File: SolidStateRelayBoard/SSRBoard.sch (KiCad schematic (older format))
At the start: 54 parts, among them J101 CONN_01X02, J102 CONN_01X02, J103 CONN_01X02, J104 CONN_01X02, J105 CONN_01X02, J106 CONN_01X02, J107 CONN_01X02, J108 CONN_01X02, J109 CONN_01X02, J110 CONN_01X02, J111 CONN_01X02, J112 CONN_01X02, J113 CONN_01X02, J114 CONN_01X02, J115 CONN_01X02, J116 CONN_01X02, J117 CONN_01X02, J118 CONN_01X02, J119 CONN_01X02, J120 CONN_01X02, J121 CONN_01X02, J122 CONN_01X02, J123 CONN_01X02, J124 CONN_01X02, J125 CONN_01X02, J126 CONN_01X02, J127 CONN_01X02, J128 CONN_01X02, J129 CONN_01X02, J130 CONN_01X02, J131 CONN_01X02, J132 CONN_01X02, J134 CONN_01X02, J135 MOUNTING_HOLE, J136 MOUNTING_HOLE, J137 MOUNTING_HOLE, J138 MOUNTING_HOLE, U101 LEDDriverSSR

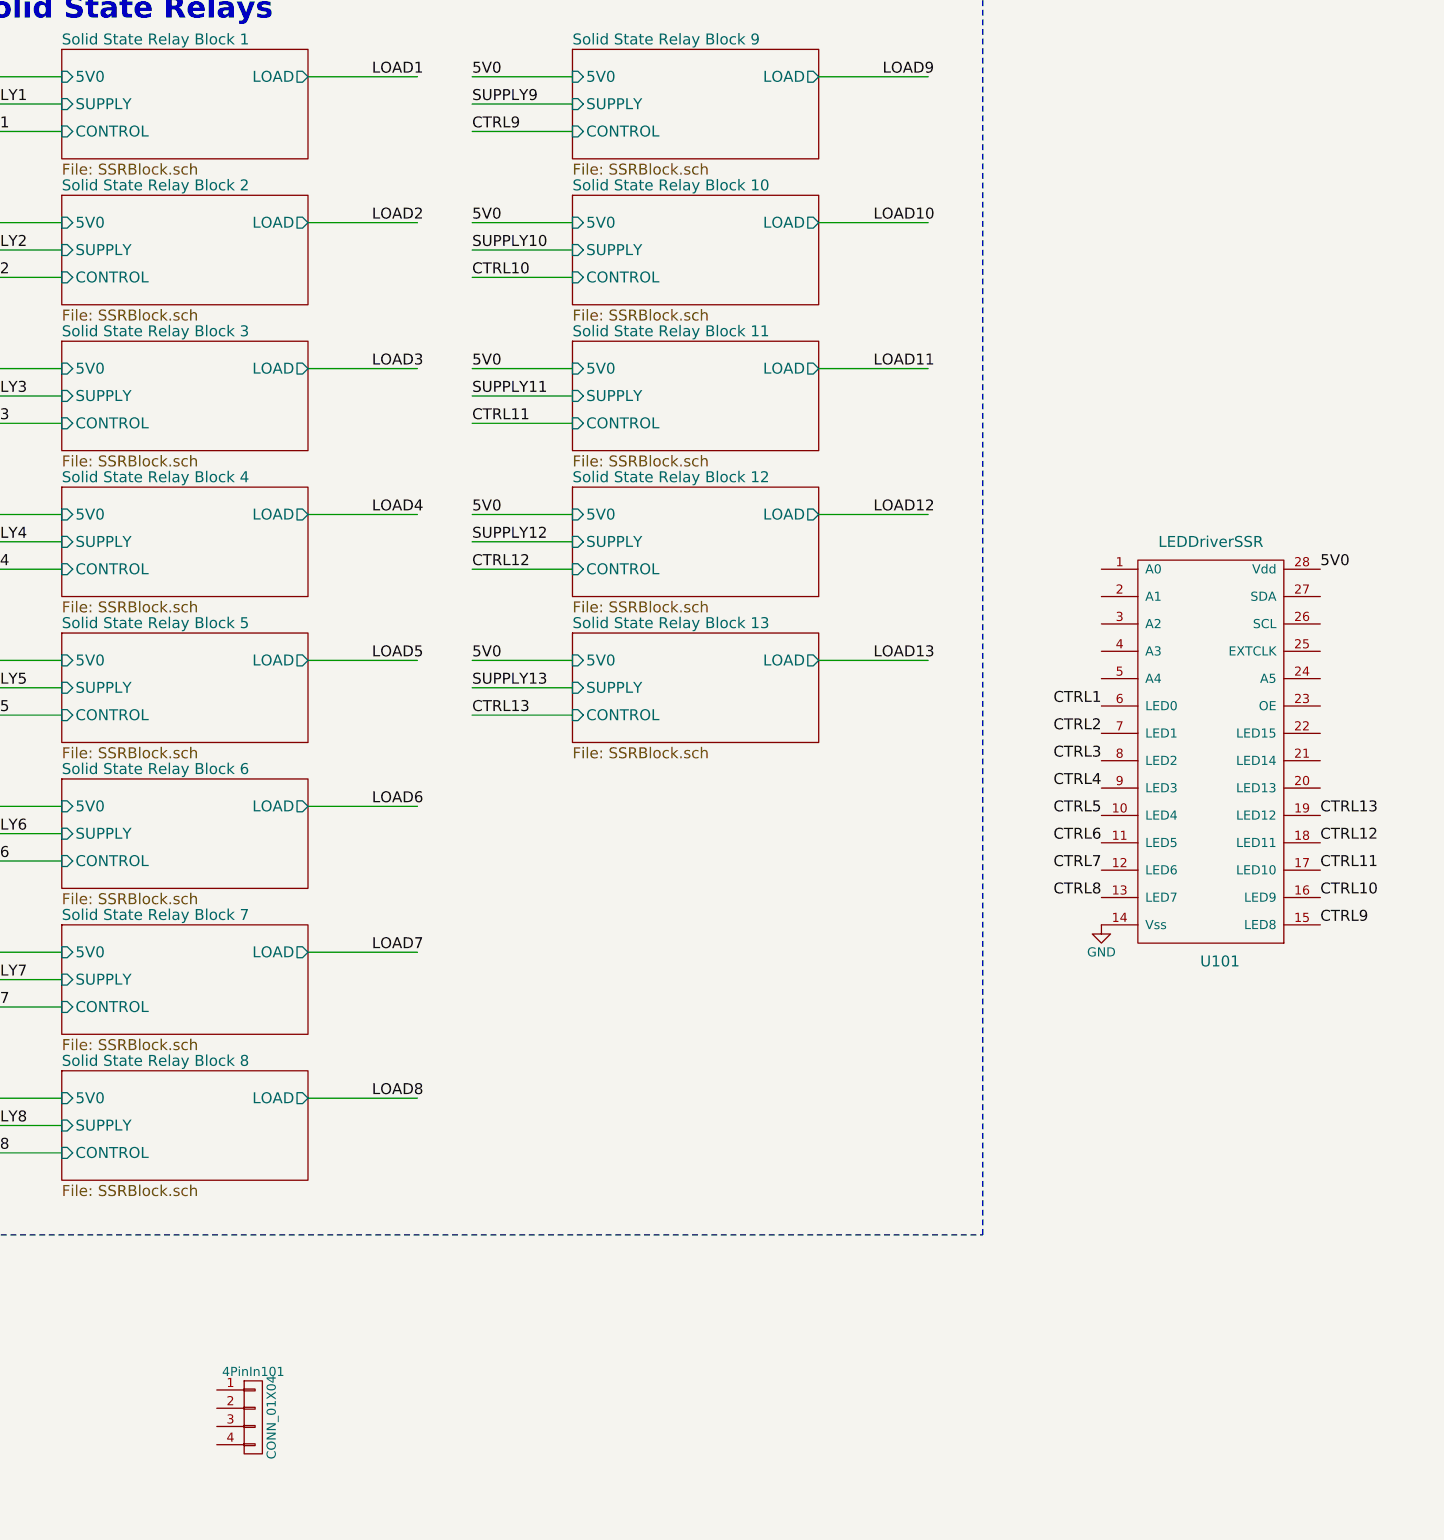
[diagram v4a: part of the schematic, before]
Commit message: Added the xtr117 to the schematic but I still need to make the footprint for it since the one on kicad is wrong.
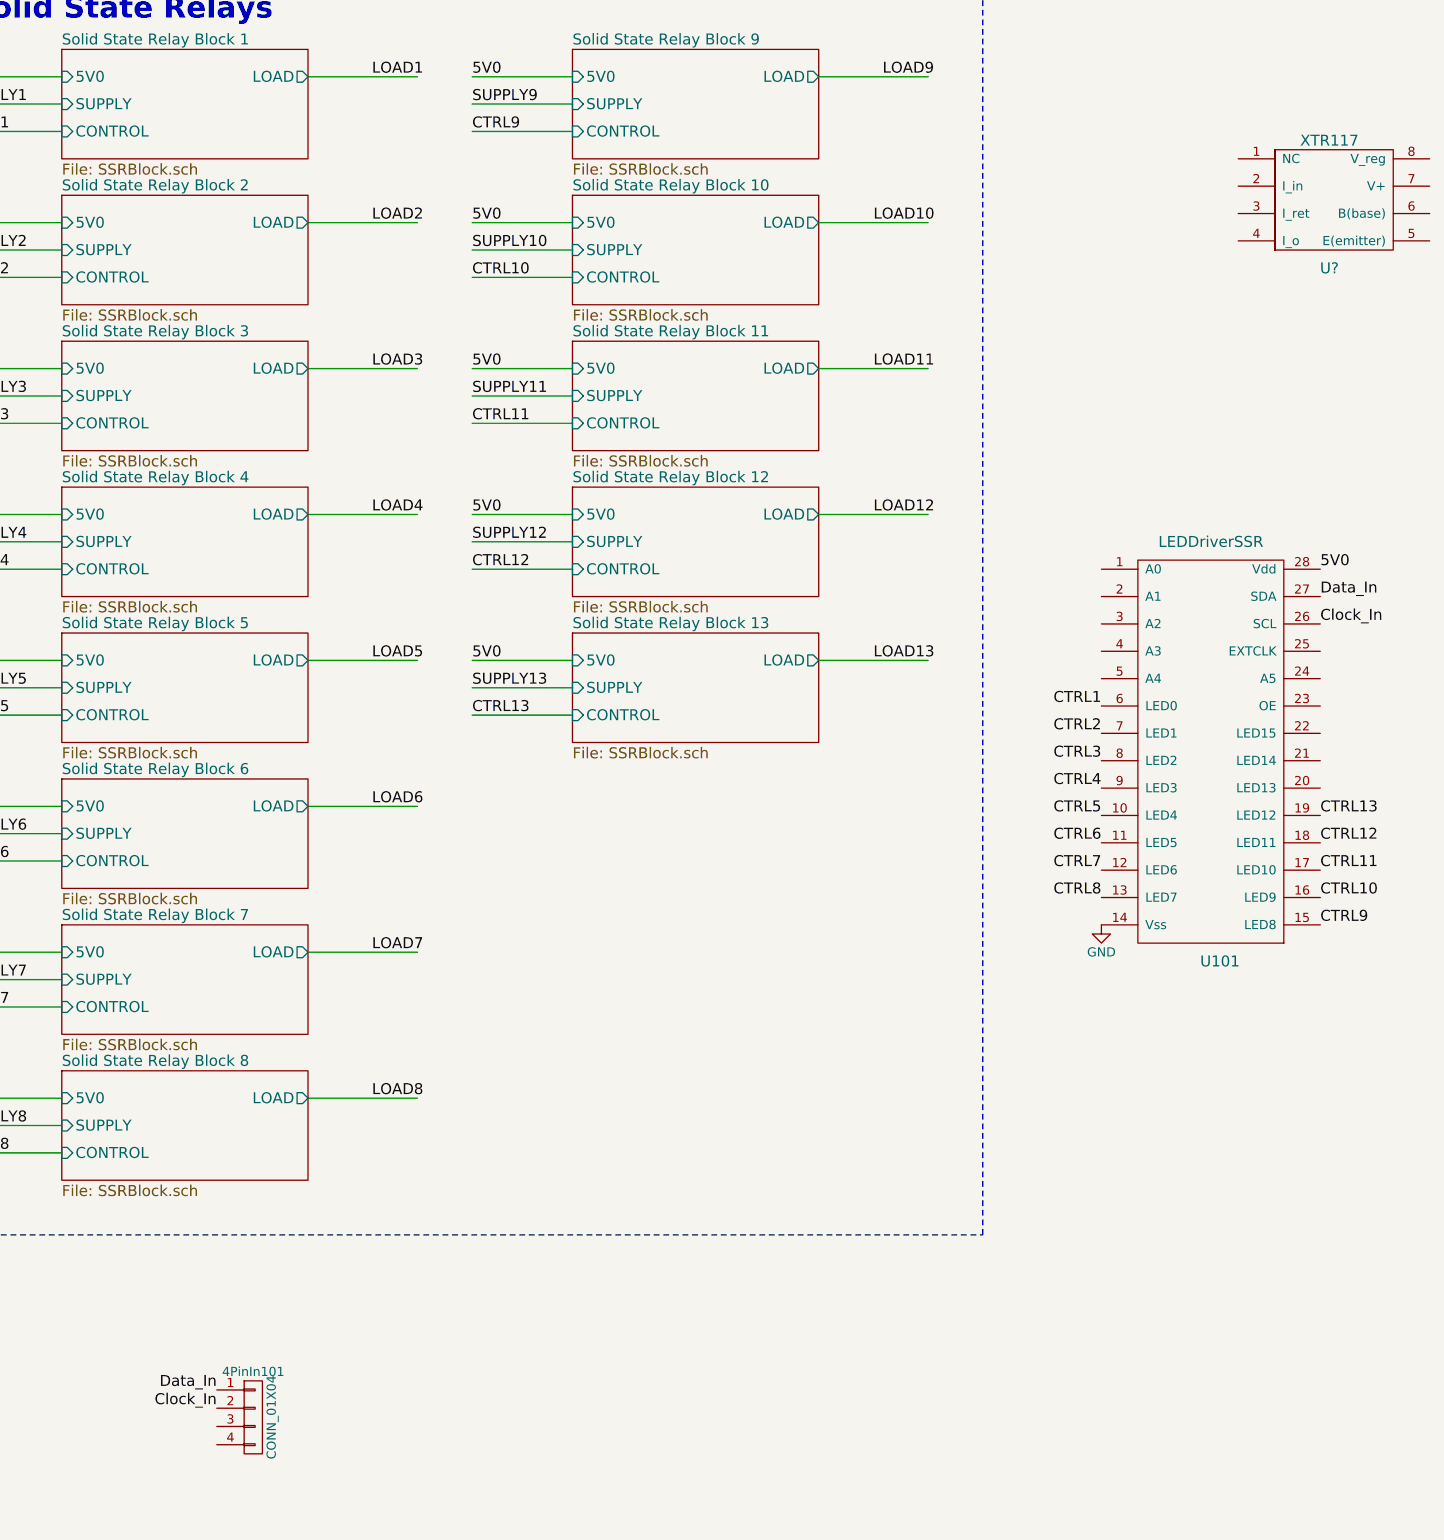
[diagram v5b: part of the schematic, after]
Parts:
- added U?: XTR117, symbol XTR117
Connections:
- net labels added: Clock_In, Data_In
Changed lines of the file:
@@
 Wire Notes Line
 	6600 500  6600 7350
+$Comp
+L XTR117 U?
+U 1 1 59143935
+P 14200 1650
+F 0 "U?" H 14200 1250 60  0000 C CNN
+F 1 "XTR117" H 14200 1950 60  0000 C CNN
+F 2 "" H 14200 2650 60  0001 C CNN
+F 3 "" H 14200 2650 60  0001 C CNN
+	1    14200 1650
+	1    0    0    -1
+$EndComp
+Text Label 8100 8200 2    60   ~ 0
+Data_In
+Text Label 8100 8300 2    60   ~ 0
+Clock_In
+Text Label 14150 3850 0    60   ~ 0
+Data_In
+Text Label 14150 4000 0    60   ~ 0
+Clock_In
 $EndSCHEMATC

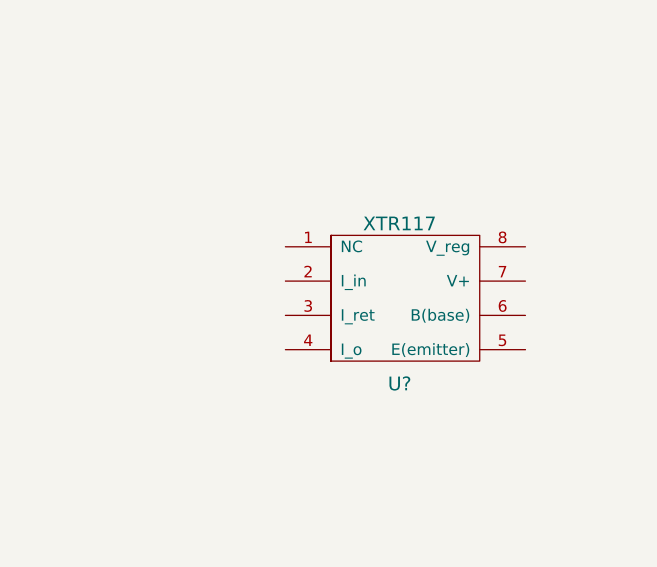
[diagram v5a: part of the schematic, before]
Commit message: Added some circuitry to the xtr117 but I’m still not sure how it should be connected. Also made slight movements to components on the pcb
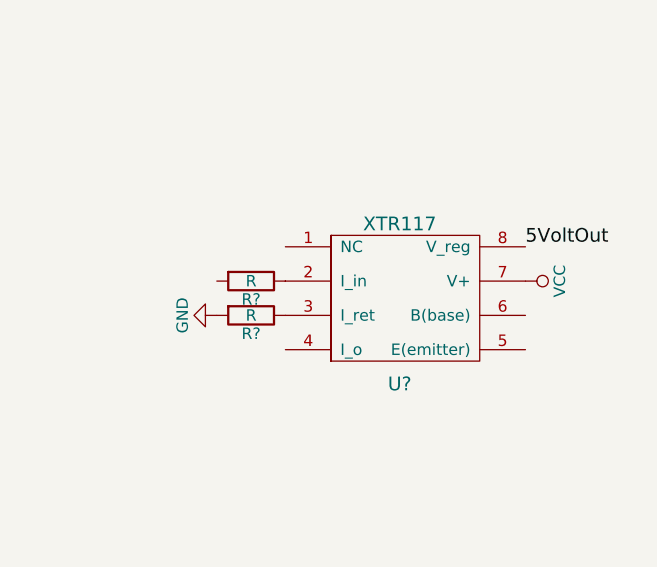
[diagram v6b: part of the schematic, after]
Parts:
- added R? (x2): R, Resistors_SMD:R_1206_HandSoldering, symbol R
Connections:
- net labels added: 5VoltOut, VCC
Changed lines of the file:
@@
 Text Label 14150 4000 0    60   ~ 0
 Clock_In
+$Comp
+L R R?
+U 1 1 591BF410
+P 13550 1600
+F 0 "R?" V 13630 1600 50  0000 C CNN
+F 1 "R" V 13550 1600 50  0000 C CNN
+F 2 "Resistors_SMD:R_1206_HandSoldering" H 13480 1600 50  0001 C CNN
+F 3 "" H 13550 1600 50  0000 C CNN
+	1    13550 1600
+	0    1    1    0
+$EndComp
+$Comp
+L R R?
+U 1 1 591BFC0E
+P 13550 1750
+F 0 "R?" V 13630 1750 50  0000 C CNN
+F 1 "R" V 13550 1750 50  0000 C CNN
+F 2 "Resistors_SMD:R_1206_HandSoldering" H 13480 1750 50  0001 C CNN
+F 3 "" H 13550 1750 50  0000 C CNN
+	1    13550 1750
+	0    1    1    0
+$EndComp
+$Comp
+L GND #PWR?
+U 1 1 591C17F1
+P 13400 1750
+F 0 "#PWR?" H 13400 1500 50  0001 C CNN
+F 1 "GND" H 13400 1600 50  0000 C CNN
+F 2 "" H 13400 1750 50  0000 C CNN
+F 3 "" H 13400 1750 50  0000 C CNN
+	1    13400 1750
+	0    1    1    0
+$EndComp
+$Comp
+L VCC #PWR?
+U 1 1 591C1DB4
+P 14750 1600
+F 0 "#PWR?" H 14750 1450 50  0001 C CNN
+F 1 "VCC" H 14750 1750 50  0000 C CNN
+F 2 "" H 14750 1600 50  0000 C CNN
+F 3 "" H 14750 1600 50  0000 C CNN
+	1    14750 1600
+	0    1    1    0
+$EndComp
+Text Label 14750 1450 0    60   ~ 0
+5VoltOut
 $EndSCHEMATC

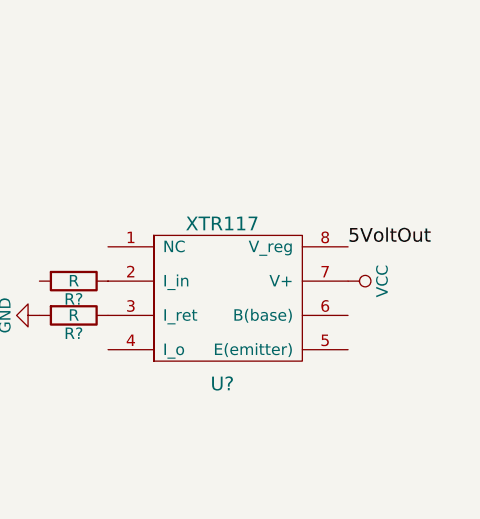
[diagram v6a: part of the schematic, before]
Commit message: changed to ppm
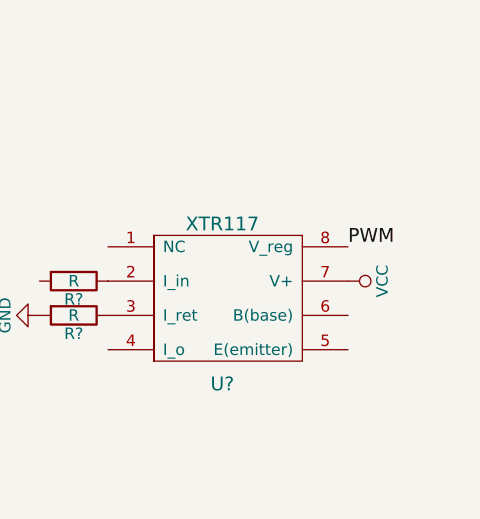
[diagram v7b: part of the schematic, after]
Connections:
- net labels added: PWM
- net labels removed: 5VoltOut
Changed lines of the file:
@@
 $EndComp
 Text Label 14750 1450 0    60   ~ 0
-5VoltOut
+PWM
 $EndSCHEMATC

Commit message: SSR Board
Misc small changes
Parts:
- removed R?: R, Resistors_SMD:R_1206_HandSoldering, symbol R
- U101: Field4 (none) -> 568-5931-1-ND
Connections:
- net labels removed: PWM, VCC
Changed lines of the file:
@@
 Text Label 14150 5650 0    60   ~ 0
 CTRL9
-Text Label 14150 5500 0    60   ~ 0
+Text Label 14150 5350 0    60   ~ 0
 CTRL10
-Text Label 14150 5350 0    60   ~ 0
+Text Label 14150 5200 0    60   ~ 0
 CTRL11
-Text Label 14150 5200 0    60   ~ 0
+Text Label 14150 5050 0    60   ~ 0
 CTRL12
-Text Label 14150 5050 0    60   ~ 0
+Text Label 14850 4450 0    60   ~ 0
 CTRL13
 Text Notes 4650 5150 0    118  ~ 24
@@
 F 2 "Housings_SSOP:TSSOP-28_4.4x9.7mm_Pitch0.65mm" H 13550 6350 60  0001 C CNN
 F 3 "" H 13550 6350 60  0001 C CNN
+F 4 "568-5931-1-ND" H 13550 4950 60  0001 C CNN "Field4"
 	1    13550 4950
 	1    0    0    -1
@@
 $EndComp
 $Comp
-L R R?
-U 1 1 591BFC0E
-P 13550 1750
-F 0 "R?" V 13630 1750 50  0000 C CNN
-F 1 "R" V 13550 1750 50  0000 C CNN
-F 2 "Resistors_SMD:R_1206_HandSoldering" H 13480 1750 50  0001 C CNN
-F 3 "" H 13550 1750 50  0000 C CNN
-	1    13550 1750
-	0    1    1    0
-$EndComp
-$Comp
 L GND #PWR?
 U 1 1 591C17F1
-P 13400 1750
-F 0 "#PWR?" H 13400 1500 50  0001 C CNN
-F 1 "GND" H 13400 1600 50  0000 C CNN
-F 2 "" H 13400 1750 50  0000 C CNN
-F 3 "" H 13400 1750 50  0000 C CNN
-	1    13400 1750
+P 13700 1750
+F 0 "#PWR?" H 13700 1500 50  0001 C CNN
+F 1 "GND" H 13700 1600 50  0000 C CNN
+F 2 "" H 13700 1750 50  0000 C CNN
+F 3 "" H 13700 1750 50  0000 C CNN
+	1    13700 1750
 	0    1    1    0
 $EndComp
-$Comp
-L VCC #PWR?
-U 1 1 591C1DB4
-P 14750 1600
-F 0 "#PWR?" H 14750 1450 50  0001 C CNN
-F 1 "VCC" H 14750 1750 50  0000 C CNN
-F 2 "" H 14750 1600 50  0000 C CNN
-F 3 "" H 14750 1600 50  0000 C CNN
-	1    14750 1600
-	0    1    1    0
-$EndComp
-Text Label 14750 1450 0    60   ~ 0
-PWM
+Text Label 14750 1600 0    60   ~ 0
+SUPPLY1
 $EndSCHEMATC
